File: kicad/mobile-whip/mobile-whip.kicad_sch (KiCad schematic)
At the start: 42 parts, among them J1 Conn_Coaxial, J2 USB_C_Receptacle_USB2.0, SW1 MK-12C02-G025, U1 LTC6268IS6, U2 TP4054, U3 LP2985-3.3

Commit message: Finalize design
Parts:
- removed D4: B5819W SL, Diode_SMD:D_SOD-123, symbol Device:D_Schottky
- removed R8: 47R, Resistor_SMD:R_1206_3216Metric, symbol Device:R
- added C10: 10nF, Capacitor_SMD:C_0805_2012Metric, symbol Device:C
- added Q1, Q2: SI2301CDS-T1-GE3, Package_TO_SOT_SMD:SOT-23, symbol Transistor_FET:AO3401A
- added R16: 330K, Resistor_SMD:R_0805_2012Metric, symbol Device:R
- added R17, R20: 5.1K, Resistor_SMD:R_0805_2012Metric, symbol Device:R
- added R18, R19: 100K, Resistor_SMD:R_0805_2012Metric, symbol Device:R
- added U4: TLV431, Package_TO_SOT_SMD:SOT-23, symbol Reference_Voltage:TL431DBZ
- C9: value 1uF/25V -> 10uF/6V3
- R10, R11, R7: value 470R -> 510R
- R15: value 47R -> 2.2R
- R9: value 47R -> 51R
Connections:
- net +BATT: now also SW1.3 (C), C10.2, Q2.2 (S); no longer BT1.1 (+)
- net GND: now also R19.1, R20.1, U4.3 (A)
- net VBUS: now also FB1.2, J2.A4 (VBUS), J2.A9 (VBUS), J2.B4 (VBUS), J2.B9 (VBUS); no longer C6.1, FB1.1, U2.4 (VCC)
- net at R10.2, R15.2: now also Q1.3 (D), R16.2; no longer SW1.2 (B)
- net at D5.2 (A): now also L2.2
- new net: R16.1, R18.1, R19.2, U4.2 (REF)
- new net: Q1.2 (S), R17.2, R18.2, SW1.2 (B)
- new net: C6.1, FB1.1, U2.4 (VCC)
- new net: BT1.1 (+), Q2.3 (D)
- new net: Q1.1 (G), R17.1, U4.1 (K)
- new net: C10.1, Q2.1 (G), R20.2
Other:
- moved on the sheet: BT1, C1, C2, C3, C4, C5, C6, C7, C8, C9, D1, D2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

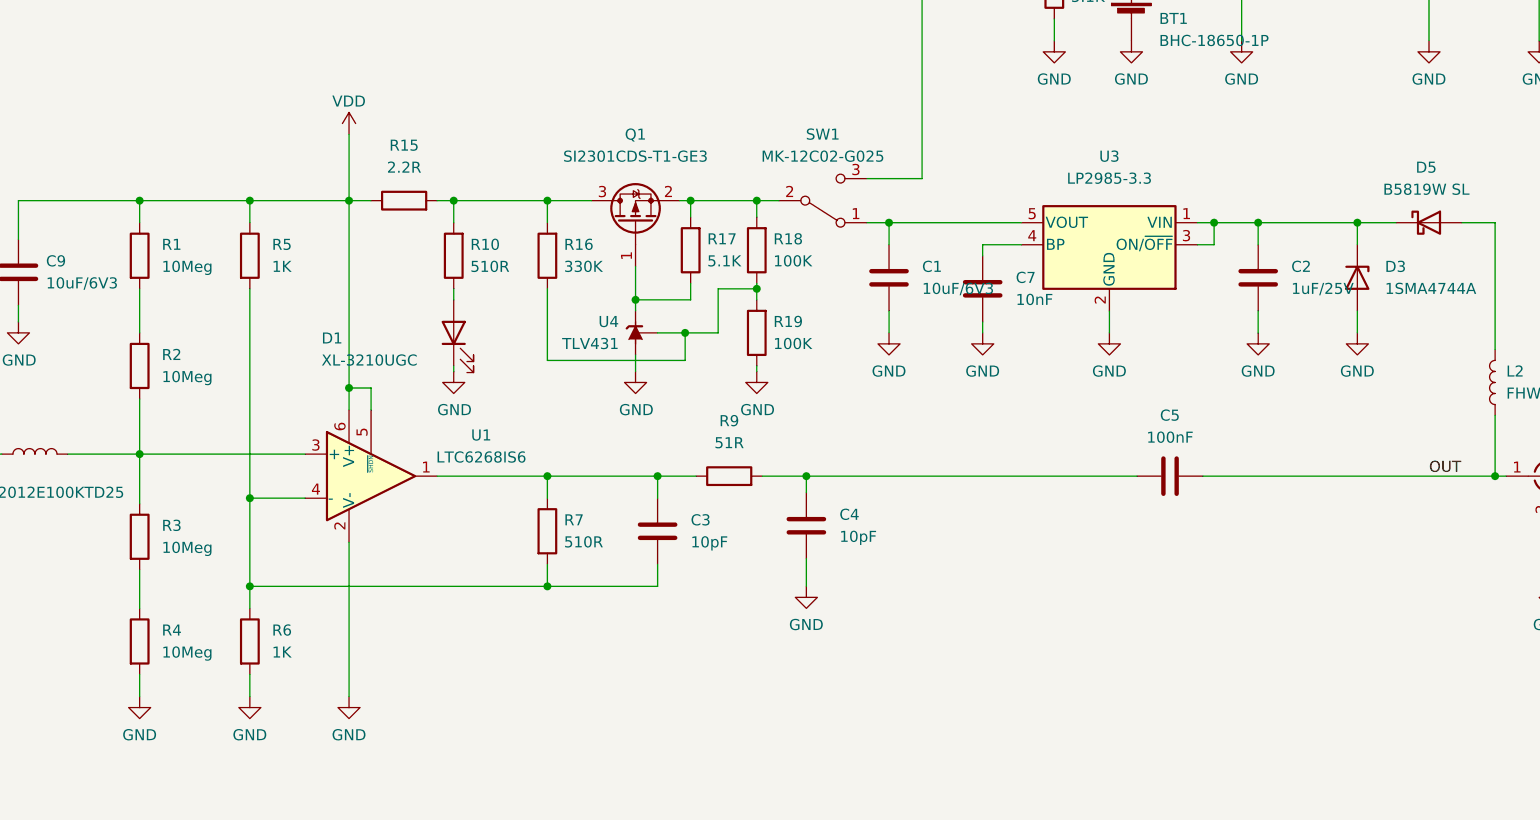
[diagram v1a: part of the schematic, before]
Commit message: Added LCSC part numbers
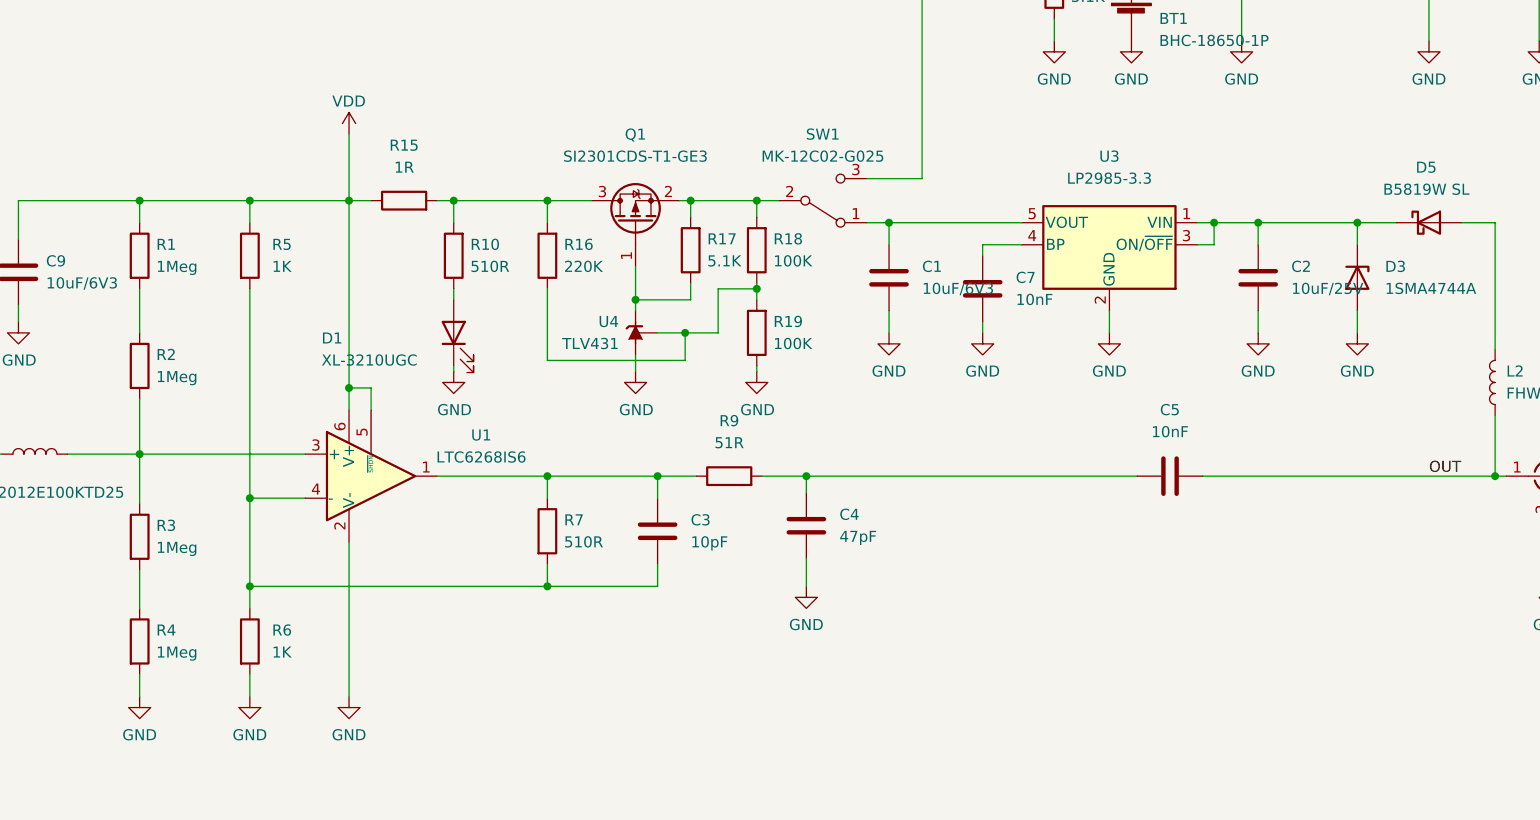
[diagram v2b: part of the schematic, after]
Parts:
- C2: value 1uF/25V -> 10uF/25V
- C4: value 10pF -> 47pF
- C5: value 100nF -> 10nF
- R1, R2, R3, R4: value 10Meg -> 1Meg
- R15: value 2.2R -> 1R; footprint Resistor_SMD:R_1206_3216Metric -> Resistor_SMD:R_0805_2012Metric
- R16: value 330K -> 220K
- R9: footprint Resistor_SMD:R_1206_3216Metric -> Resistor_SMD:R_0805_2012Metric
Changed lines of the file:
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@@
       (effects (font (size 1.27 1.27)) (justify right))
     )
-    (property "Value" "330K" (id 1) (at 99.06 87.6299 0)
+    (property "Value" "220K" (id 1) (at 99.06 87.6299 0)
       (effects (font (size 1.27 1.27)) (justify right))
     )
@@
       (effects (font (size 1.27 1.27)) (justify left))
     )
-    (property "Value" "10pF" (id 1) (at 130.81 118.7449 0)
+    (property "Value" "47pF" (id 1) (at 130.81 118.7449 0)
       (effects (font (size 1.27 1.27)) (justify left))
     )
@@
   (symbol (lib_id "Device:C") (at 168.91 111.76 90) (unit 1)
     (in_bom yes) (on_board yes) (fields_autoplaced)
-    (property "Reference" "C5" (id 0) (at 168.91 104.775 90))
-    (property "Value" "100nF" (id 1) (at 168.91 107.315 90))
+    (property "Reference" "C5" (id 0) (at 168.91 104.14 90))
+    (property "Value" "10nF" (id 1) (at 168.91 106.68 90))
     (property "Footprint" "Capacitor_SMD:C_0805_2012Metric" (id 2) (at 172.72 110.7948 0)
       (effects (font (size 1.27 1.27)) hide)
@@
   (symbol (lib_id "Device:R") (at 50.165 118.745 0) (unit 1)
     (in_bom yes) (on_board yes) (fields_autoplaced)
-    (property "Reference" "R3" (id 0) (at 52.705 117.4749 0)
-      (effects (font (size 1.27 1.27)) (justify left))
-    )
-    (property "Value" "10Meg" (id 1) (at 52.705 120.0149 0)
+    (property "Reference" "R3" (id 0) (at 52.07 117.4749 0)
+      (effects (font (size 1.27 1.27)) (justify left))
+    )
+    (property "Value" "1Meg" (id 1) (at 52.07 120.0149 0)
       (effects (font (size 1.27 1.27)) (justify left))
     )
@@
     (in_bom yes) (on_board yes)
     (property "Reference" "R15" (id 0) (at 80.645 73.66 90))
-    (property "Value" "2.2R" (id 1) (at 80.645 76.2 90))
-    (property "Footprint" "Resistor_SMD:R_1206_3216Metric" (id 2) (at 80.645 81.788 90)
+    (property "Value" "1R" (id 1) (at 80.645 76.2 90))
+    (property "Footprint" "Resistor_SMD:R_0805_2012Metric" (id 2) (at 80.645 81.788 90)
       (effects (font (size 1.27 1.27)) hide)
     )
@@
   (symbol (lib_id "Device:R") (at 50.165 99.06 0) (unit 1)
     (in_bom yes) (on_board yes) (fields_autoplaced)
-    (property "Reference" "R2" (id 0) (at 52.705 97.7899 0)
-      (effects (font (size 1.27 1.27)) (justify left))
-    )
-    (property "Value" "10Meg" (id 1) (at 52.705 100.3299 0)
+    (property "Reference" "R2" (id 0) (at 52.07 97.7899 0)
+      (effects (font (size 1.27 1.27)) (justify left))
+    )
+    (property "Value" "1Meg" (id 1) (at 52.07 100.3299 0)
       (effects (font (size 1.27 1.27)) (justify left))
     )
@@
     (property "Reference" "R9" (id 0) (at 118.11 105.41 90))
     (property "Value" "51R" (id 1) (at 118.11 107.95 90))
-    (property "Footprint" "Resistor_SMD:R_1206_3216Metric" (id 2) (at 118.11 113.538 90)
+    (property "Footprint" "Resistor_SMD:R_0805_2012Metric" (id 2) (at 118.11 113.538 90)
       (effects (font (size 1.27 1.27)) hide)
     )
@@
   (symbol (lib_id "Device:R") (at 50.165 130.81 0) (unit 1)
     (in_bom yes) (on_board yes) (fields_autoplaced)
-    (property "Reference" "R4" (id 0) (at 52.705 129.5399 0)
-      (effects (font (size 1.27 1.27)) (justify left))
-    )
-    (property "Value" "10Meg" (id 1) (at 52.705 132.0799 0)
+    (property "Reference" "R4" (id 0) (at 52.07 129.5399 0)
+      (effects (font (size 1.27 1.27)) (justify left))
+    )
+    (property "Value" "1Meg" (id 1) (at 52.07 132.0799 0)
       (effects (font (size 1.27 1.27)) (justify left))
     )
@@
       (effects (font (size 1.27 1.27)) (justify left))
     )
-    (property "Value" "1uF/25V" (id 1) (at 182.88 90.1699 0)
+    (property "Value" "10uF/25V" (id 1) (at 182.88 90.1699 0)
       (effects (font (size 1.27 1.27)) (justify left))
     )
@@
   (symbol (lib_id "Device:R") (at 50.165 86.36 0) (unit 1)
     (in_bom yes) (on_board yes) (fields_autoplaced)
-    (property "Reference" "R1" (id 0) (at 52.705 85.0899 0)
-      (effects (font (size 1.27 1.27)) (justify left))
-    )
-    (property "Value" "10Meg" (id 1) (at 52.705 87.6299 0)
+    (property "Reference" "R1" (id 0) (at 52.07 85.0899 0)
+      (effects (font (size 1.27 1.27)) (justify left))
+    )
+    (property "Value" "1Meg" (id 1) (at 52.07 87.6299 0)
       (effects (font (size 1.27 1.27)) (justify left))
     )
@@
     )
     (path "/e1d0f007-dbb1-4e39-bddb-b296c1f695b2"
-      (reference "C2") (unit 1) (value "1uF/25V") (footprint "Capacitor_SMD:C_0805_2012Metric")
+      (reference "C2") (unit 1) (value "10uF/25V") (footprint "Capacitor_SMD:C_0805_2012Metric")
     )
     (path "/6c408477-374e-46a4-b195-223418296e20"
@@
     )
     (path "/2675271d-548a-409a-9942-989ed6de53e0"
-      (reference "C4") (unit 1) (value "10pF") (footprint "Capacitor_SMD:C_0805_2012Metric")
+      (reference "C4") (unit 1) (value "47pF") (footprint "Capacitor_SMD:C_0805_2012Metric")
     )
     (path "/3c5248a3-8f3f-476f-a470-b075e2a60306"
-      (reference "C5") (unit 1) (value "100nF") (footprint "Capacitor_SMD:C_0805_2012Metric")
+      (reference "C5") (unit 1) (value "10nF") (footprint "Capacitor_SMD:C_0805_2012Metric")
     )
     (path "/2dbfcc83-037d-45d3-a843-f93d44828d77"
@@
     )
     (path "/e9794b2a-e1b3-44a0-b872-cc35efa61991"
-      (reference "R1") (unit 1) (value "10Meg") (footprint "Resistor_SMD:R_0805_2012Metric")
+      (reference "R1") (unit 1) (value "1Meg") (footprint "Resistor_SMD:R_0805_2012Metric")
     )
     (path "/99dd2ec6-179e-423d-81e7-0ea2ae6fd053"
-      (reference "R2") (unit 1) (value "10Meg") (footprint "Resistor_SMD:R_0805_2012Metric")
+      (reference "R2") (unit 1) (value "1Meg") (footprint "Resistor_SMD:R_0805_2012Metric")
     )
     (path "/5b42686a-82f2-4da4-bade-a02dd9ec8eb8"
-      (reference "R3") (unit 1) (value "10Meg") (footprint "Resistor_SMD:R_0805_2012Metric")
+      (reference "R3") (unit 1) (value "1Meg") (footprint "Resistor_SMD:R_0805_2012Metric")
     )
     (path "/af8730ba-4aca-4759-9b8d-e74032efa187"
-      (reference "R4") (unit 1) (value "10Meg") (footprint "Resistor_SMD:R_0805_2012Metric")
+      (reference "R4") (unit 1) (value "1Meg") (footprint "Resistor_SMD:R_0805_2012Metric")
     )
     (path "/1878959e-e5a0-4826-844b-8f80ab886b5a"
@@
     )
     (path "/a493556d-5c89-4b22-8fa7-8d9eb52a51f3"
-      (reference "R9") (unit 1) (value "51R") (footprint "Resistor_SMD:R_1206_3216Metric")
+      (reference "R9") (unit 1) (value "51R") (footprint "Resistor_SMD:R_0805_2012Metric")
     )
     (path "/21334618-8ea5-486c-b9b5-5dfbd4e69037"
@@
     )
     (path "/659f8832-2273-4ff7-99bc-c38687c2d0b6"
-      (reference "R15") (unit 1) (value "2.2R") (footprint "Resistor_SMD:R_1206_3216Metric")
+      (reference "R15") (unit 1) (value "1R") (footprint "Resistor_SMD:R_0805_2012Metric")
     )
     (path "/0edb349a-538e-45fa-9791-63c08496ed81"
-      (reference "R16") (unit 1) (value "330K") (footprint "Resistor_SMD:R_0805_2012Metric")
+      (reference "R16") (unit 1) (value "220K") (footprint "Resistor_SMD:R_0805_2012Metric")
     )
     (path "/4a67e278-f47a-4845-af84-74140b10b744"

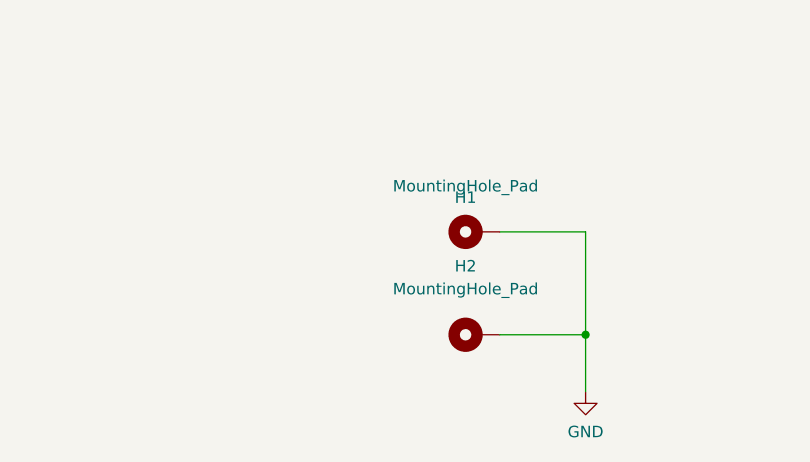
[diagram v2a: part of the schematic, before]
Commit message: Add tooling holes
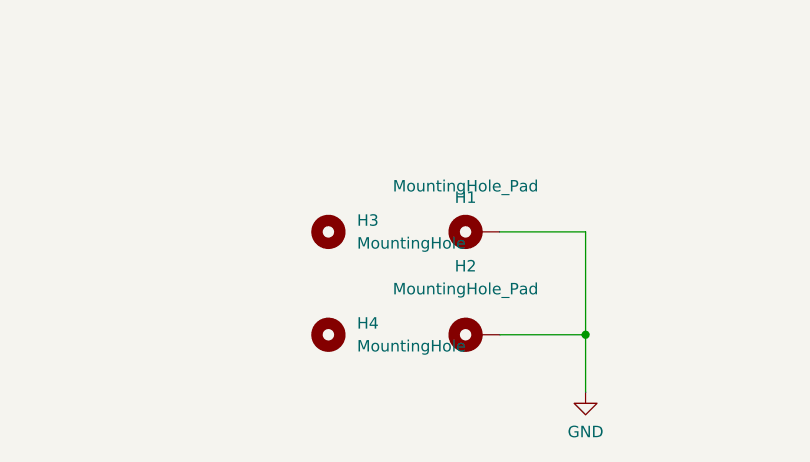
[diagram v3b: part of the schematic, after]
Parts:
- added H3, H4: MountingHole, project:TOOLING-HOLE, symbol Mechanical:MountingHole
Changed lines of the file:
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@@
     (pin "2")
+  )
+  (symbol (lib_id "Mechanical:MountingHole") (at 130.175 162.56 0) (unit 1)
+    (in_bom yes) (on_board yes) (fields_autoplaced)
+    (property "Reference" "H3" (id 0) (at 133.35 161.2899 0)
+      (effects (font (size 1.27 1.27)) (justify left))
+    )
+    (property "Value" "MountingHole" (id 1) (at 133.35 163.8299 0)
+      (effects (font (size 1.27 1.27)) (justify left))
+    )
+    (property "Footprint" "project:TOOLING-HOLE" (id 2) (at 130.175 162.56 0)
+      (effects (font (size 1.27 1.27)) hide)
+    )
+    (property "Datasheet" "~" (id 3) (at 130.175 162.56 0)
+      (effects (font (size 1.27 1.27)) hide)
+    )
   )
   (symbol (lib_id "Device:C") (at 109.855 118.11 0) (unit 1)
@@
     (pin "2")
   )
+  (symbol (lib_id "Mechanical:MountingHole") (at 130.175 173.99 0) (unit 1)
+    (in_bom yes) (on_board yes) (fields_autoplaced)
+    (property "Reference" "H4" (id 0) (at 133.35 172.7199 0)
+      (effects (font (size 1.27 1.27)) (justify left))
+    )
+    (property "Value" "MountingHole" (id 1) (at 133.35 175.2599 0)
+      (effects (font (size 1.27 1.27)) (justify left))
+    )
+    (property "Footprint" "project:TOOLING-HOLE" (id 2) (at 130.175 173.99 0)
+      (effects (font (size 1.27 1.27)) hide)
+    )
+    (property "Datasheet" "~" (id 3) (at 130.175 173.99 0)
+      (effects (font (size 1.27 1.27)) hide)
+    )
+  )
   (symbol (lib_id "power:GND") (at 62.865 137.16 0) (unit 1)
     (in_bom yes) (on_board yes) (fields_autoplaced)
@@
       (reference "H2") (unit 1) (value "MountingHole_Pad") (footprint "MountingHole:MountingHole_3.2mm_M3_ISO7380_Pad_TopBottom")
     )
+    (path "/6884c1b4-ba74-400a-b15a-2bf546c04e73"
+      (reference "H3") (unit 1) (value "MountingHole") (footprint "project:TOOLING-HOLE")
+    )
+    (path "/da492421-a211-4983-b0d9-f67dcbbbad16"
+      (reference "H4") (unit 1) (value "MountingHole") (footprint "project:TOOLING-HOLE")
+    )
     (path "/5ec3bd07-85f5-47e9-a70f-b13f8032dfa2"

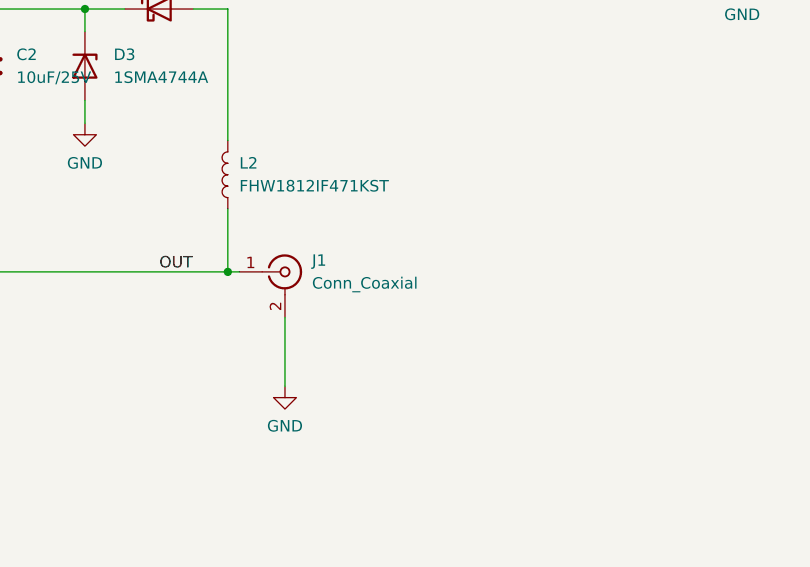
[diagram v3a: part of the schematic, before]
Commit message: Added component value to SMA connector
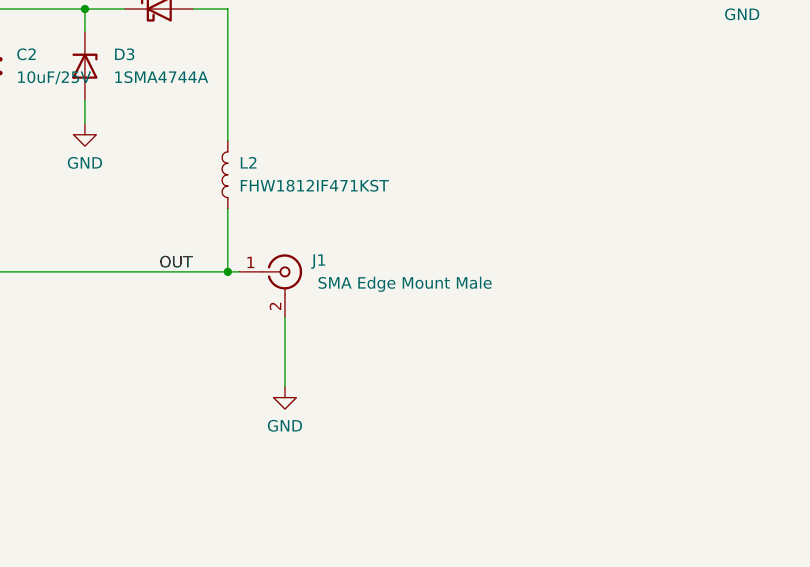
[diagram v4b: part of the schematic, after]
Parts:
- J1: value Conn_Coaxial -> SMA Edge Mount Male
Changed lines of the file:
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@@
     (in_bom yes) (on_board yes)
     (property "Reference" "J1" (id 0) (at 216.535 110.49 0))
-    (property "Value" "Conn_Coaxial" (id 1) (at 221.615 113.03 0))
+    (property "Value" "SMA Edge Mount Male" (id 1) (at 226.06 113.03 0))
     (property "Footprint" "project:SMA_Male_EdgeMount" (id 2) (at 212.725 111.76 0)
       (effects (font (size 1.27 1.27)) hide)
@@
     )
     (path "/5ec3bd07-85f5-47e9-a70f-b13f8032dfa2"
-      (reference "J1") (unit 1) (value "Conn_Coaxial") (footprint "project:SMA_Male_EdgeMount")
+      (reference "J1") (unit 1) (value "SMA Edge Mount Male") (footprint "project:SMA_Male_EdgeMount")
     )
     (path "/0b361c8c-c7f3-45c6-b828-350b331fec0c"
